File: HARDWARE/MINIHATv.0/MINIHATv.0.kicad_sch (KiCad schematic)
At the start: 0 parts

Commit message: Merge branch 'main' into display-basic-implementation
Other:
- added sheet Ethernet (Ethernet.kicad_sch)
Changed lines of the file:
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@@
 	(paper "A4")
+	(sheet
+		(at 96.52 92.71)
+		(size 30.48 20.32)
+		(exclude_from_sim no)
+		(in_bom yes)
+		(on_board yes)
+		(dnp no)
+		(fields_autoplaced yes)
+		(stroke
+			(width 0.1524)
+			(type solid)
+		)
+		(fill
+			(color 0 0 0 0)
+		)
+		(property "Sheetname" "Ethernet"
+			(at 96.52 91.9984 0)
+			(show_name no)
+			(do_not_autoplace no)
+			(effects
+				(font
+					(size 1.27 1.27)
+				)
+				(justify left bottom)
+			)
+		)
+		(property "Sheetfile" "Ethernet.kicad_sch"
+			(at 96.52 113.6146 0)
+			(show_name no)
+			(do_not_autoplace no)
+			(effects
+				(font
+					(size 1.27 1.27)
+				)
+				(justify left top)
+			)
+		)
+		(instances
+			(project "MINIHATv.0"
+				(path "/19041ef4-1d16-4363-8780-721ad9f20b33"
+					(page "4")
+				)
+			)
+		)
+	)
 	(sheet
 		(at 95.25 50.8)

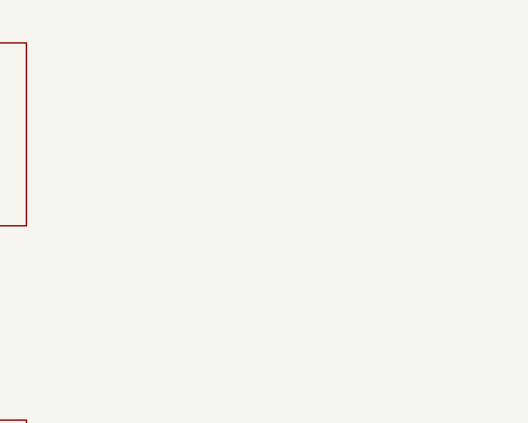
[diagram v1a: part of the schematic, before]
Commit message: added can sheet
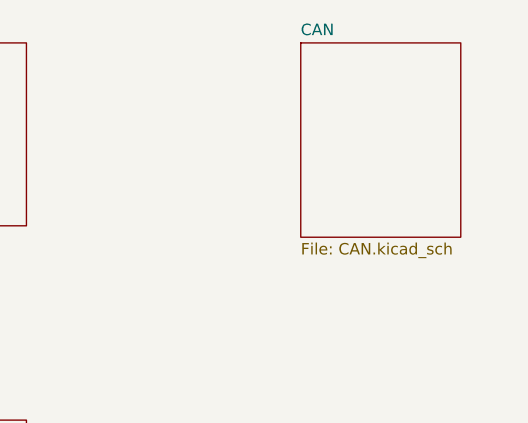
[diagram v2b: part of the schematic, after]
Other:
- added sheet CAN (CAN.kicad_sch)
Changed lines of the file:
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@@
 	(paper "A4")
+	(sheet
+		(at 157.48 50.8)
+		(size 17.78 21.59)
+		(exclude_from_sim no)
+		(in_bom yes)
+		(on_board yes)
+		(dnp no)
+		(fields_autoplaced yes)
+		(stroke
+			(width 0.1524)
+			(type solid)
+		)
+		(fill
+			(color 0 0 0 0)
+		)
+		(property "Sheetname" "CAN"
+			(at 157.48 50.0884 0)
+			(show_name no)
+			(do_not_autoplace no)
+			(effects
+				(font
+					(size 1.27 1.27)
+				)
+				(justify left bottom)
+			)
+		)
+		(property "Sheetfile" "CAN.kicad_sch"
+			(at 157.48 72.9746 0)
+			(show_name no)
+			(do_not_autoplace no)
+			(effects
+				(font
+					(size 1.27 1.27)
+				)
+				(justify left top)
+			)
+		)
+		(instances
+			(project "MINIHATv.0"
+				(path "/19041ef4-1d16-4363-8780-721ad9f20b33"
+					(page "3")
+				)
+			)
+		)
+	)
 	(sheet
 		(at 96.52 92.71)

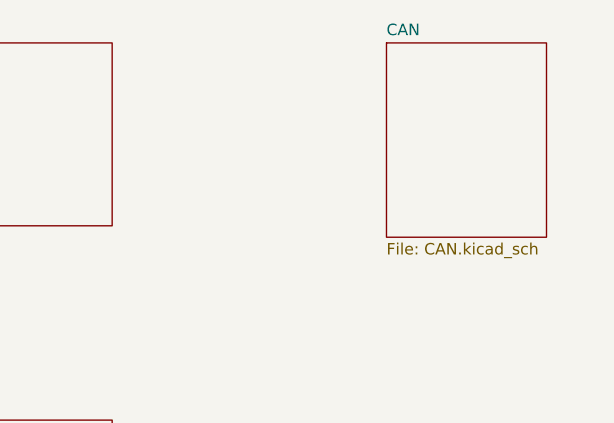
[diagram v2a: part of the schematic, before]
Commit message: CAN schematic circuit added
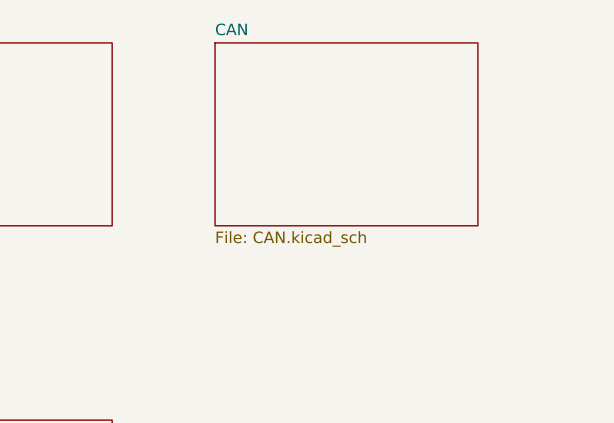
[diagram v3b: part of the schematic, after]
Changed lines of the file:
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@@
 	(paper "A4")
 	(sheet
-		(at 157.48 50.8)
-		(size 17.78 21.59)
+		(at 138.43 50.8)
+		(size 29.21 20.32)
 		(exclude_from_sim no)
 		(in_bom yes)
@@
 		)
 		(property "Sheetname" "CAN"
-			(at 157.48 50.0884 0)
+			(at 138.43 50.0884 0)
 			(show_name no)
 			(do_not_autoplace no)
@@
 		)
 		(property "Sheetfile" "CAN.kicad_sch"
-			(at 157.48 72.9746 0)
+			(at 138.43 71.7046 0)
 			(show_name no)
 			(do_not_autoplace no)

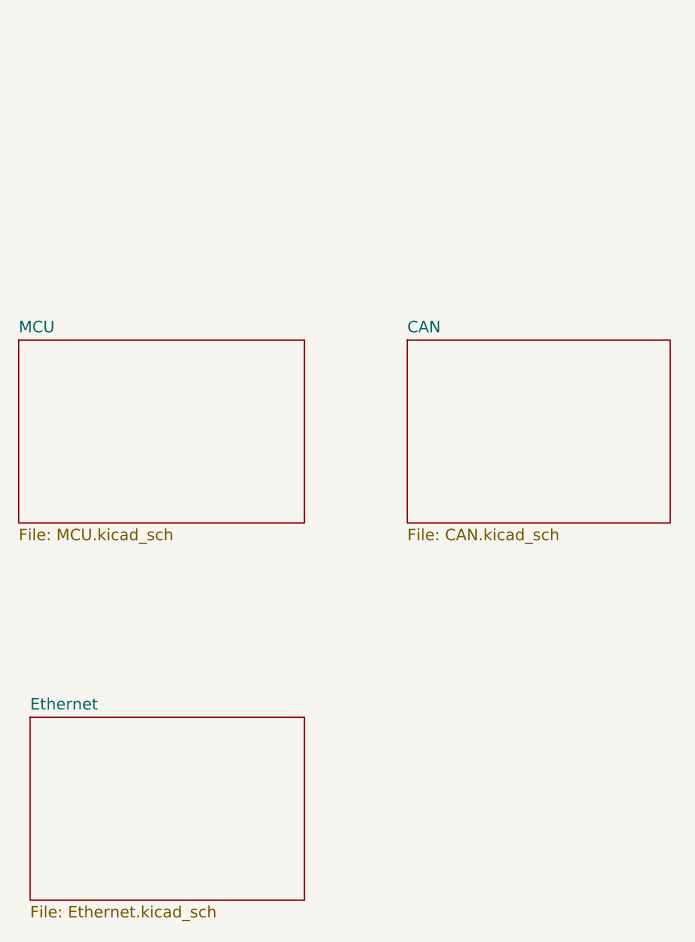
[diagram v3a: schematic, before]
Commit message: added HDMI page
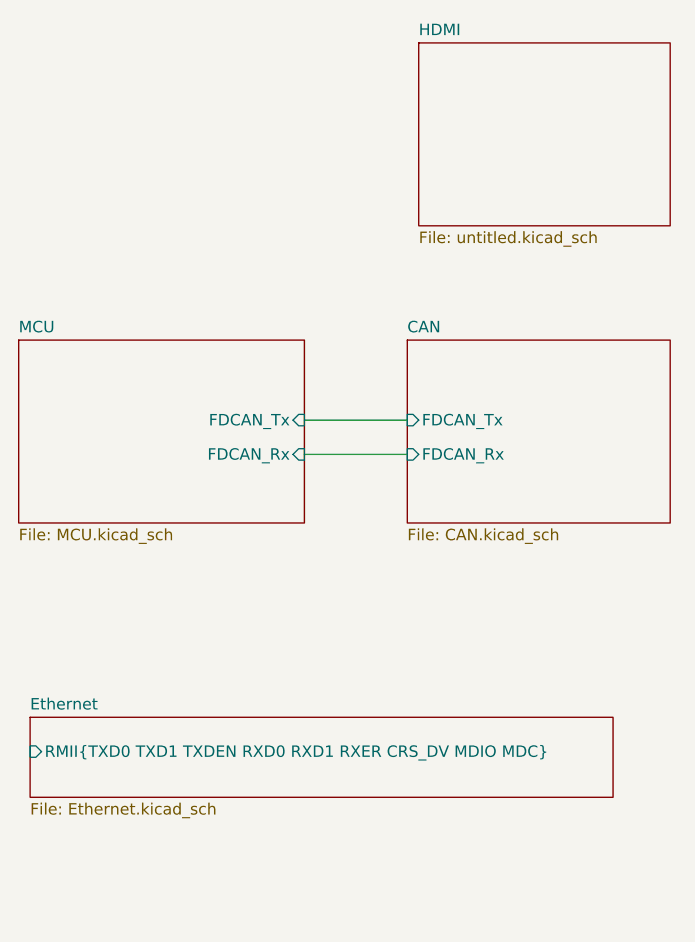
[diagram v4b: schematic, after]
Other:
- added sheet HDMI (untitled.kicad_sch)
- sheet CAN ports: added FDCAN_Rx, FDCAN_Tx; removed none
- sheet Ethernet ports: added RMII{TXD0 TXD1 TXDEN RXD0 RXD1 RXER CRS_DV MDIO MDC}; removed none
- sheet MCU ports: added FDCAN_Rx, FDCAN_Tx; removed none
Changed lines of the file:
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@@
 	(generator_version "10.0")
 	(paper "A4")
+	(wire
+		(pts
+			(xy 127 59.69) (xy 138.43 59.69)
+		)
+		(stroke
+			(width 0)
+			(type default)
+		)
+	)
+	(wire
+		(pts
+			(xy 127 63.5) (xy 138.43 63.5)
+		)
+		(stroke
+			(width 0)
+			(type default)
+		)
+	)
 	(sheet
 		(at 138.43 50.8)
@@
 				)
 				(justify left top)
+			)
+		)
+		(pin "FDCAN_Rx" input
+			(at 138.43 63.5 180)
+			(effects
+				(font
+					(size 1.27 1.27)
+				)
+				(justify left)
+			)
+		)
+		(pin "FDCAN_Tx" input
+			(at 138.43 59.69 180)
+			(effects
+				(font
+					(size 1.27 1.27)
+				)
+				(justify left)
 			)
 		)
@@
 	)
 	(sheet
+		(at 139.7 17.78)
+		(size 27.94 20.32)
+		(exclude_from_sim no)
+		(in_bom yes)
+		(on_board yes)
+		(dnp no)
+		(fields_autoplaced yes)
+		(stroke
+			(width 0.1524)
+			(type solid)
+		)
+		(fill
+			(color 0 0 0 0)
+		)
+		(property "Sheetname" "HDMI"
+			(at 139.7 17.0684 0)
+			(show_name no)
+			(do_not_autoplace no)
+			(effects
+				(font
+					(size 1.27 1.27)
+				)
+				(justify left bottom)
+			)
+		)
+		(property "Sheetfile" "untitled.kicad_sch"
+			(at 139.7 38.6846 0)
+			(show_name no)
+			(do_not_autoplace no)
+			(effects
+				(font
+					(size 1.27 1.27)
+				)
+				(justify left top)
+			)
+		)
+		(instances
+			(project "MINIHATv.0"
+				(path "/19041ef4-1d16-4363-8780-721ad9f20b33"
+					(page "5")
+				)
+			)
+		)
+	)
+	(sheet
 		(at 96.52 92.71)
-		(size 30.48 20.32)
+		(size 64.77 8.89)
 		(exclude_from_sim no)
 		(in_bom yes)
@@
 		)
 		(property "Sheetfile" "Ethernet.kicad_sch"
-			(at 96.52 113.6146 0)
-			(show_name no)
-			(do_not_autoplace no)
-			(effects
-				(font
-					(size 1.27 1.27)
-				)
-				(justify left top)
+			(at 96.52 102.1846 0)
+			(show_name no)
+			(do_not_autoplace no)
+			(effects
+				(font
+					(size 1.27 1.27)
+				)
+				(justify left top)
+			)
+		)
+		(pin "RMII{TXD0 TXD1 TXDEN RXD0 RXD1 RXER CRS_DV MDIO MDC}" input
+			(at 96.52 96.52 180)
+			(effects
+				(font
+					(size 1.27 1.27)
+				)
+				(justify left)
 			)
 		)
@@
 			)
 		)
+		(pin "FDCAN_Rx" input
+			(at 127 63.5 0)
+			(effects
+				(font
+					(size 1.27 1.27)
+				)
+				(justify right)
+			)
+		)
+		(pin "FDCAN_Tx" input
+			(at 127 59.69 0)
+			(effects
+				(font
+					(size 1.27 1.27)
+				)
+				(justify right)
+			)
+		)

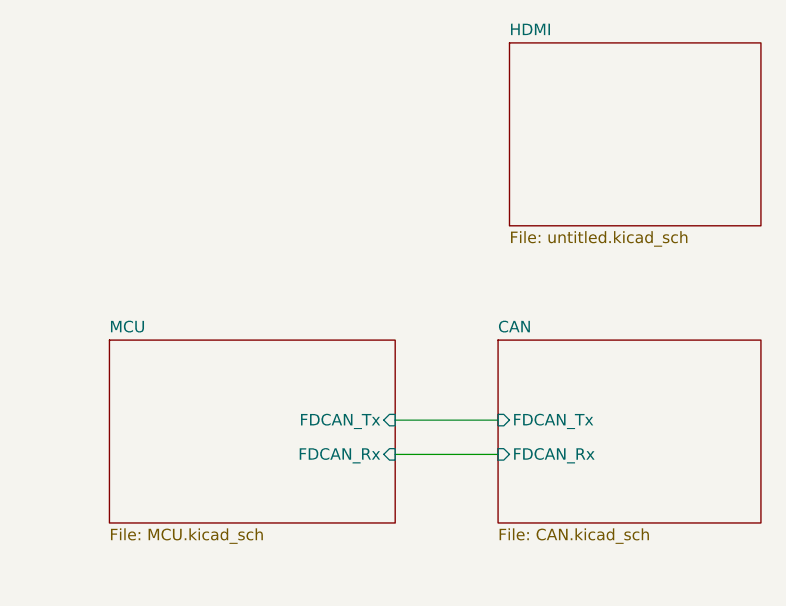
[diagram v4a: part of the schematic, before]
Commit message: TFP to MCU connection added, TFP config pins tied
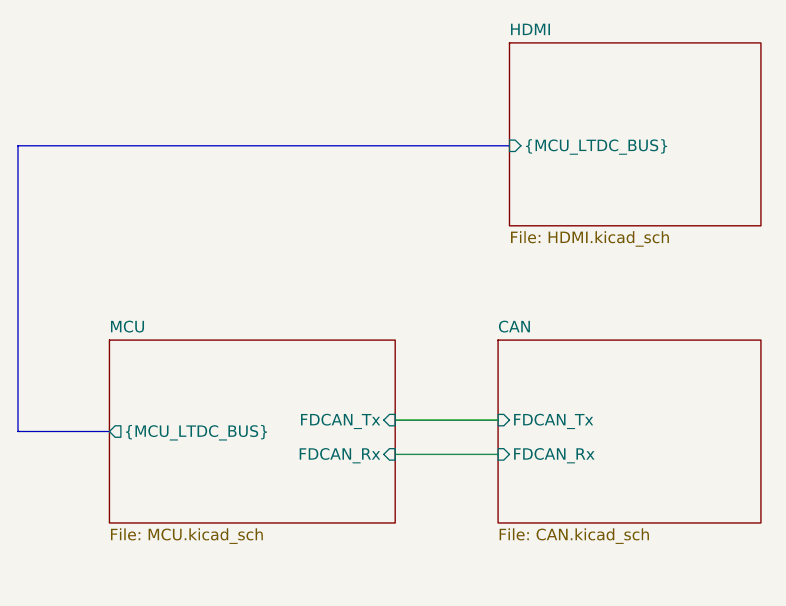
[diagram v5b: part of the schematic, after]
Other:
- sheet HDMI: file untitled.kicad_sch -> HDMI.kicad_sch
- sheet HDMI ports: added {MCU_LTDC_BUS}; removed none
- sheet MCU ports: added {MCU_LTDC_BUS}; removed none
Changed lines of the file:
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@@
+		)
+	)
+	(bus
+		(pts
+			(xy 85.09 60.96) (xy 95.25 60.96)
+		)
+		(stroke
+			(width 0)
+			(type default)
+		)
+	)
+	(bus
+		(pts
+			(xy 85.09 29.21) (xy 85.09 60.96)
+		)
+		(stroke
+			(width 0)
+			(type default)
+		)
+	)
+	(bus
+		(pts
+			(xy 139.7 29.21) (xy 85.09 29.21)
+		)
+		(stroke
+			(width 0)
+			(type default)
 		)
 	)
@@
 			)
 		)
-		(property "Sheetfile" "untitled.kicad_sch"
+		(property "Sheetfile" "HDMI.kicad_sch"
 			(at 139.7 38.6846 0)
 			(show_name no)
@@
 				)
 				(justify left top)
+			)
+		)
+		(pin "{MCU_LTDC_BUS}" input
+			(at 139.7 29.21 180)
+			(effects
+				(font
+					(size 1.27 1.27)
+				)
+				(justify left)
 			)
 		)
@@
 			)
 		)
+		(pin "{MCU_LTDC_BUS}" output
+			(at 95.25 60.96 180)
+			(effects
+				(font
+					(size 1.27 1.27)
+				)
+				(justify left)
+			)
+		)

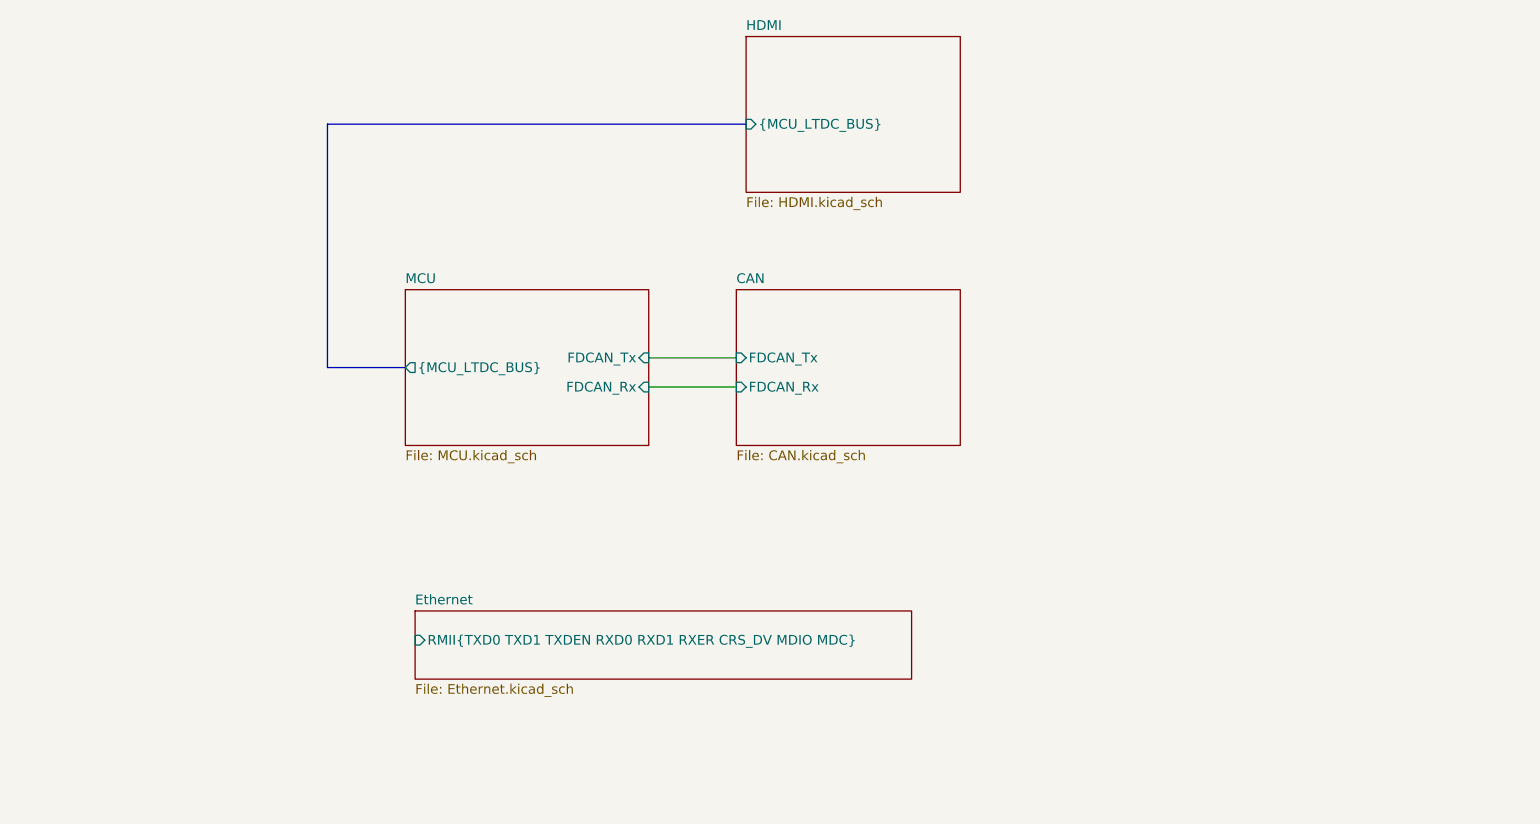
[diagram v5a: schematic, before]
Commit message: FTDI for debbug added to MCU
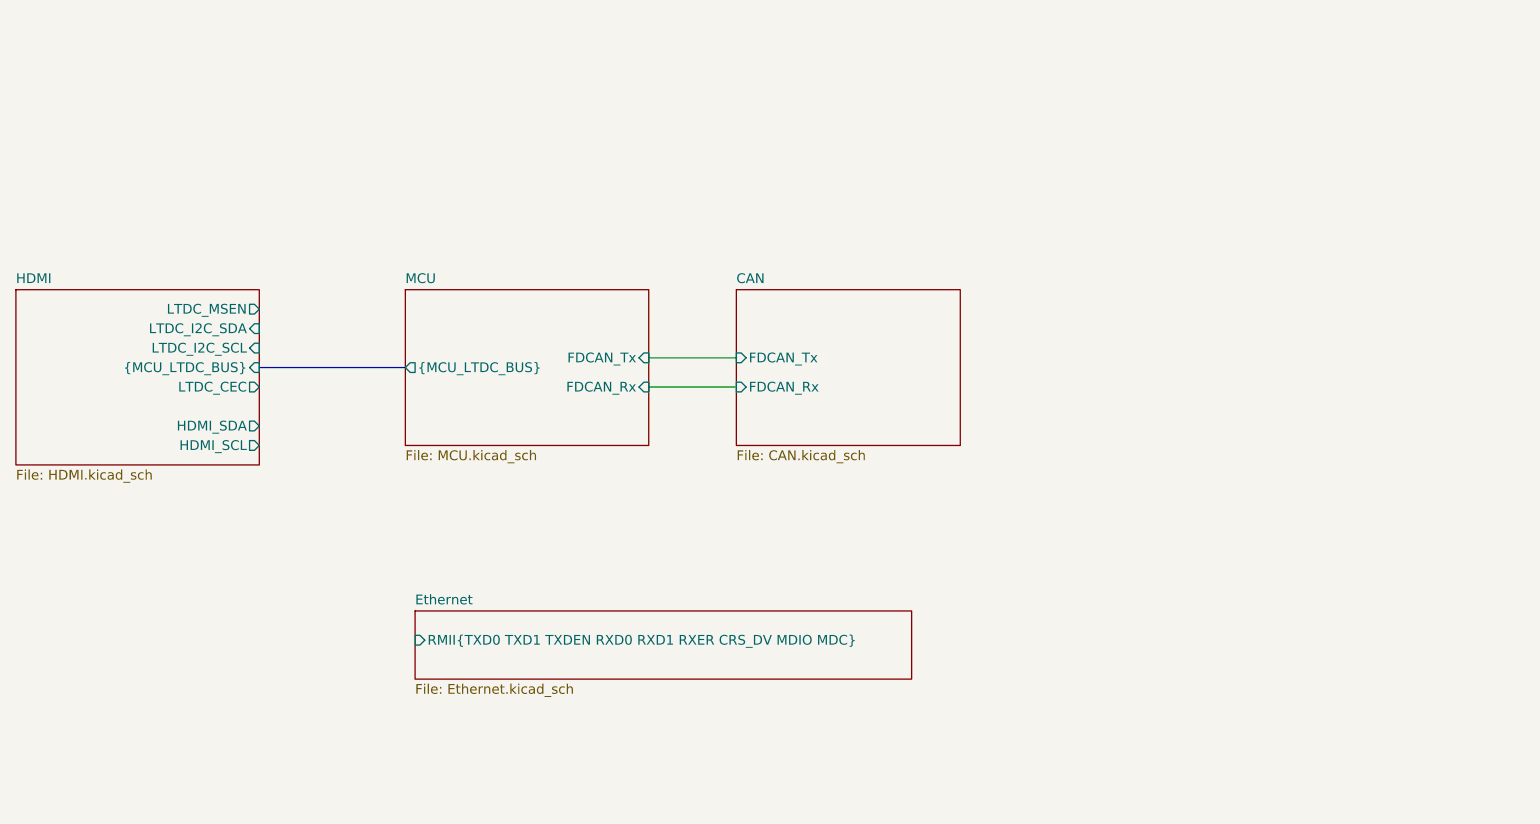
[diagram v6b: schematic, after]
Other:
- sheet HDMI ports: added HDMI_SCL, HDMI_SDA, LTDC_CEC, LTDC_I2C_SCL, LTDC_I2C_SDA, LTDC_MSEN; removed none
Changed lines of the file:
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@@
 		)
 	)
-	(bus
+	(wire
 		(pts
-			(xy 85.09 60.96) (xy 95.25 60.96)
+			(xy 127 63.5) (xy 138.43 63.5)
 		)
 		(stroke
@@
 	(bus
 		(pts
-			(xy 85.09 29.21) (xy 85.09 60.96)
-		)
-		(stroke
-			(width 0)
-			(type default)
-		)
-	)
-	(bus
-		(pts
-			(xy 139.7 29.21) (xy 85.09 29.21)
-		)
-		(stroke
-			(width 0)
-			(type default)
-		)
-	)
-	(wire
-		(pts
-			(xy 127 63.5) (xy 138.43 63.5)
+			(xy 76.2 60.96) (xy 95.25 60.96)
 		)
 		(stroke
@@
 	)
 	(sheet
-		(at 139.7 17.78)
-		(size 27.94 20.32)
+		(at 44.45 50.8)
+		(size 31.75 22.86)
 		(exclude_from_sim no)
 		(in_bom yes)
@@
 		)
 		(property "Sheetname" "HDMI"
-			(at 139.7 17.0684 0)
+			(at 44.45 50.0884 0)
 			(show_name no)
 			(do_not_autoplace no)
@@
 		)
 		(property "Sheetfile" "HDMI.kicad_sch"
-			(at 139.7 38.6846 0)
+			(at 44.45 74.2446 0)
 			(show_name no)
 			(do_not_autoplace no)
@@
 		)
 		(pin "{MCU_LTDC_BUS}" input
-			(at 139.7 29.21 180)
+			(at 76.2 60.96 0)
 			(effects
 				(font
 					(size 1.27 1.27)
 				)
-				(justify left)
+				(justify right)
 			)
 		)
+		(pin "HDMI_SCL" output
+			(at 76.2 71.12 0)
+			(effects
+				(font
+					(size 1.27 1.27)
+				)
+				(justify right)
+			)
+		)
+		(pin "HDMI_SDA" output
+			(at 76.2 68.58 0)
+			(effects
+				(font
+					(size 1.27 1.27)
+				)
+				(justify right)
+			)
+		)
+		(pin "LTDC_CEC" output
+			(at 76.2 63.5 0)
+			(effects
+				(font
+					(size 1.27 1.27)
+				)
+				(justify right)
+			)
+		)
+		(pin "LTDC_I2C_SCL" input
+			(at 76.2 58.42 0)
+			(effects
+				(font
+					(size 1.27 1.27)
+				)
+				(justify right)
+			)
+		)
+		(pin "LTDC_I2C_SDA" input
+			(at 76.2 55.88 0)
+			(effects
+				(font
+					(size 1.27 1.27)
+				)
+				(justify right)
+			)
+		)
+		(pin "LTDC_MSEN" output
+			(at 76.2 53.34 0)
+			(effects
+				(font
+					(size 1.27 1.27)
+				)
+				(justify right)
+			)
+		)

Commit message: added BT sheet and created BT schemat symbol
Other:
- added sheet Bluetooth (Bluetooth.kicad_sch)
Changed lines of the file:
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@@
+	)
+	(sheet
+		(at 96.52 17.78)
+		(size 31.75 22.86)
+		(exclude_from_sim no)
+		(in_bom yes)
+		(on_board yes)
+		(dnp no)
+		(fields_autoplaced yes)
+		(stroke
+			(width 0.1524)
+			(type solid)
+		)
+		(fill
+			(color 0 0 0 0)
+		)
+		(property "Sheetname" "Bluetooth"
+			(at 96.52 17.0684 0)
+			(show_name no)
+			(do_not_autoplace no)
+			(effects
+				(font
+					(size 1.27 1.27)
+				)
+				(justify left bottom)
+			)
+		)
+		(property "Sheetfile" "Bluetooth.kicad_sch"
+			(at 96.52 41.2246 0)
+			(show_name no)
+			(do_not_autoplace no)
+			(effects
+				(font
+					(size 1.27 1.27)
+				)
+				(justify left top)
+			)
+		)
+		(instances
+			(project "MINIHATv.0"
+				(path "/19041ef4-1d16-4363-8780-721ad9f20b33"
+					(page "6")
+				)
+			)
+		)
 	)
 	(sheet
